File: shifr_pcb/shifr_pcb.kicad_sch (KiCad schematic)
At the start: 93 parts, among them SW1 Power Switch, SW2 Reset Switch, U1 Nice_Nano_V2

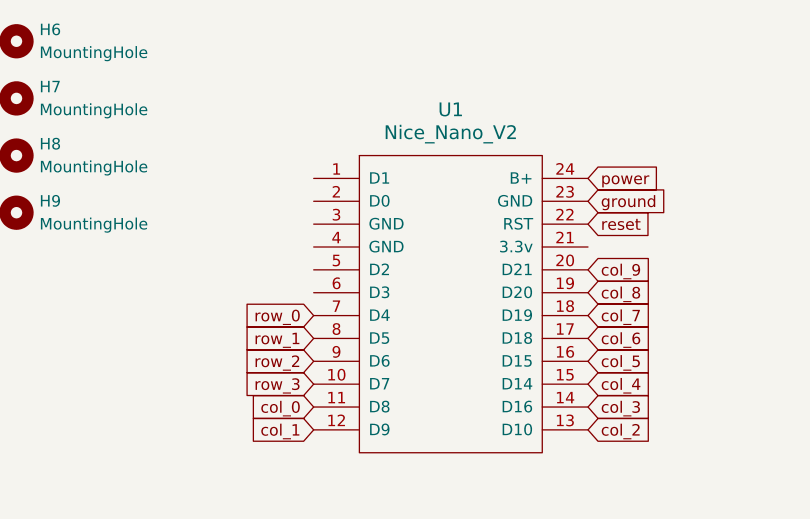
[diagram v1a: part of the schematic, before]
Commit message: Changed power switch footprint
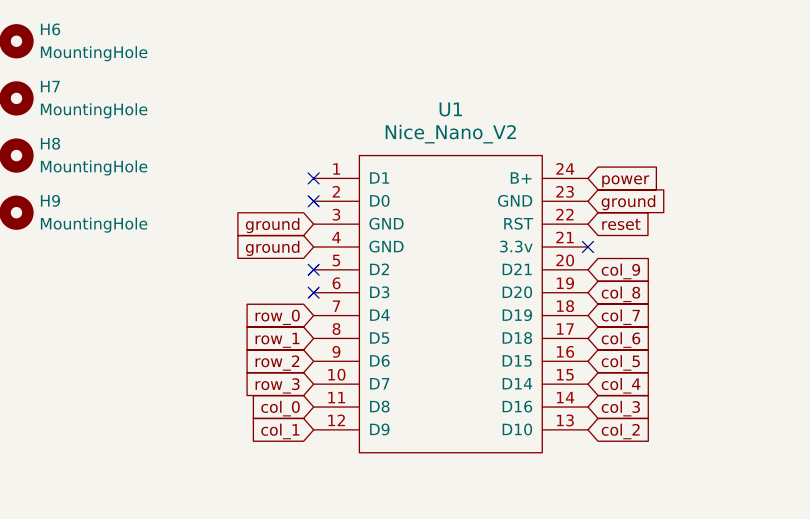
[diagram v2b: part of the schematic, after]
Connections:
- net ground: now also U1.3 (GND), U1.4 (GND)
- no-connect marks 0 -> 5
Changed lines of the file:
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@@
 		(color 0 0 0 0)
 	)
+	(no_connect
+		(at 77.47 44.45)
+	)
+	(no_connect
+		(at 77.47 54.61)
+	)
+	(no_connect
+		(at 77.47 41.91)
+	)
+	(no_connect
+		(at 107.95 49.53)
+	)
+	(no_connect
+		(at 77.47 52.07)
+	)
 	(wire
 		(pts
@@
 		)
 	)
+	(global_label "ground"
+		(shape input)
+		(at 77.47 49.53 180)
+		(fields_autoplaced yes)
+		(effects
+			(font
+				(size 1.27 1.27)
+			)
+			(justify right)
+		)
+		(property "Intersheetrefs" "${INTERSHEET_REFS}"
+			(at 67.9536 49.53 0)
+			(effects
+				(font
+					(size 1.27 1.27)
+				)
+				(justify right)
+				(hide yes)
+			)
+		)
+	)
 	(global_label "col_4"
 		(shape input)
@@
 				(hide yes)
 			)
+		)
+	)
+	(global_label "ground"
+		(shape input)
+		(at 77.47 46.99 180)
+		(fields_autoplaced yes)
+		(effects
+			(font
+				(size 1.27 1.27)
+			)
+			(justify right)
+		)
+		(property "Intersheetrefs" "${INTERSHEET_REFS}"
+			(at 67.9536 46.99 0)
+			(effects
+				(font
+					(size 1.27 1.27)
+				)
+				(justify right)
+				(hide yes)
+			)

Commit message: update main pcb
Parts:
- removed H1, H2, H3, H4, H5: MountingHole, MountingHole:MountingHole_2.2mm_M2_Pad_Via, symbol Mechanical:MountingHole
- removed H6, H7, H8, H9: MountingHole, MountingHole:MountingHole_2.2mm_M2_ISO14580, symbol Mechanical:MountingHole
